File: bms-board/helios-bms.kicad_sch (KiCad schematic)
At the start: 61 parts, among them J1 Debug, J2 Umbilical, J3 Output, Q1 PMOS, Q2 NMOS, U1 TPS22811, U2 BQ25306, U3 STM32L011F4Ux, U4 THVD1400D, U6 TPS563207s

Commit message: components selected
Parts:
- removed J1: Debug, symbol Connector_Generic:Conn_01x05
- removed J2: Umbilical, symbol Connector_Generic:Conn_01x04
- added J1: Debug, Connector_PinHeader_1.27mm:PinHeader_2x05_P1.27mm_Vertical_SMD, symbol Connector_Generic:Conn_02x05_Odd_Even
- added J3: Umbilical, Connector_JST:JST_ZE_SM04B-ZESS-TB_1x04-1MP_P1.50mm_Horizontal, symbol Connector_Generic_MountingPin:Conn_01x04_MountingPin
- C1: renamed from C10; footprint (none) -> Capacitor_SMD:C_0603_1608Metric
- C10: renamed from C4; footprint (none) -> Capacitor_SMD:C_0603_1608Metric
- C11: renamed from C23; value 100u -> 470u; footprint (none) -> Capacitor_SMD:CP_Elec_10x10
- C12: renamed from C5; footprint (none) -> Capacitor_SMD:C_0402_1005Metric
- C13: renamed from C14; footprint (none) -> Capacitor_SMD:C_0402_1005Metric
- C14: renamed from C15; footprint (none) -> Capacitor_SMD:C_0402_1005Metric
- C15: renamed from C6; footprint (none) -> Capacitor_SMD:C_0402_1005Metric
- C16: renamed from C7; footprint (none) -> Capacitor_SMD:C_0402_1005Metric
- C17: renamed from C19; footprint (none) -> Capacitor_SMD:C_0603_1608Metric
- C18: renamed from C16; footprint (none) -> Capacitor_SMD:C_0402_1005Metric
- C19: renamed from C8; footprint (none) -> Capacitor_SMD:C_0603_1608Metric
- C2: renamed from C11; footprint (none) -> Capacitor_SMD:C_0402_1005Metric
- C20: renamed from C18; footprint (none) -> Capacitor_SMD:C_0402_1005Metric
- C21: renamed from C9; footprint (none) -> Capacitor_SMD:C_0603_1608Metric
- C22: renamed from C17; footprint (none) -> Capacitor_SMD:C_0603_1608Metric
- C23: renamed from C3; footprint (none) -> Capacitor_SMD:C_0402_1005Metric
- C3: renamed from C20; footprint (none) -> Capacitor_SMD:C_0402_1005Metric
- C4: renamed from C1; footprint (none) -> Capacitor_SMD:C_0402_1005Metric
- C5: renamed from C21; footprint (none) -> Capacitor_SMD:C_0402_1005Metric
- C6: renamed from C2; footprint (none) -> Capacitor_SMD:C_0402_1005Metric
- C7: renamed from C12; footprint (none) -> Capacitor_SMD:C_0402_1005Metric
- C8: renamed from C13; footprint (none) -> Capacitor_SMD:C_0603_1608Metric
- C9: renamed from C22; footprint (none) -> Capacitor_SMD:C_0402_1005Metric
- D1: footprint (none) -> LED_SMD:LED_0402_1005Metric
- J2: renamed from J3; footprint (none) -> Connector_JST:JST_ZE_SM03B-ZESS-TB_1x03-1MP_P1.50mm_Horizontal; symbol Connector_Generic:Conn_01x03 -> Connector_Generic_MountingPin:Conn_01x03_MountingPin
- L1: footprint (none) -> Inductor_SMD:L_Taiyo-Yuden_NR-50xx
- L2: footprint (none) -> Inductor_SMD:L_0805_2012Metric
- Q1: renamed from Q2; footprint (none) -> Helios-BMS:SOT-1220_UDFN6B_TOS-L; symbol Simulation_SPICE:NMOS -> Helios-BMS:SSM6K388NU
- Q2: renamed from Q1; value PMOS -> SSM3J332R; footprint (none) -> Helios-BMS:SOT-1220_UDFN6B_TOS-L; symbol Simulation_SPICE:PMOS -> Helios-BMS:SSM6J507NU
- R1: renamed from R23; footprint (none) -> Resistor_SMD:R_0402_1005Metric
- R10: renamed from R20; footprint (none) -> Resistor_SMD:R_0402_1005Metric
- R11: renamed from R21; value 50k -> 49.9k; footprint (none) -> Resistor_SMD:R_0402_1005Metric
- R12: renamed from R22; footprint (none) -> Resistor_SMD:R_0402_1005Metric
- R13: renamed from R10; footprint (none) -> Resistor_SMD:R_0402_1005Metric
- R14: renamed from R9; value TBD -> 300; footprint (none) -> Resistor_SMD:R_0402_1005Metric
- R15: renamed from R1; footprint (none) -> Resistor_SMD:R_0402_1005Metric
- R16: renamed from R2; footprint (none) -> Resistor_SMD:R_0402_1005Metric
- R17: renamed from R12; footprint (none) -> Resistor_SMD:R_0402_1005Metric
- R18: renamed from R11; footprint (none) -> Resistor_SMD:R_0402_1005Metric
- R19: renamed from R13; footprint (none) -> Resistor_SMD:R_0402_1005Metric
- R2: renamed from R3; footprint (none) -> Resistor_SMD:R_0402_1005Metric
- R20: renamed from R14; footprint (none) -> Resistor_SMD:R_0402_1005Metric
- R21: renamed from R15; footprint (none) -> Resistor_SMD:R_0402_1005Metric
- R22: renamed from R7; footprint (none) -> Resistor_SMD:R_0402_1005Metric
- R23: renamed from R8; footprint (none) -> Resistor_SMD:R_0402_1005Metric
- R24: footprint (none) -> Resistor_SMD:R_0402_1005Metric
- R3: renamed from R4; footprint (none) -> Resistor_SMD:R_0402_1005Metric
- R4: renamed from R17; footprint (none) -> Resistor_SMD:R_0402_1005Metric
- R5: renamed from R18; footprint (none) -> Resistor_SMD:R_0402_1005Metric
- R6: renamed from R19; footprint (none) -> Resistor_SMD:R_0402_1005Metric
- R7: renamed from R5; value 135k -> 137k; footprint (none) -> Resistor_SMD:R_0402_1005Metric
- R8: renamed from R6; footprint (none) -> Resistor_SMD:R_0402_1005Metric
- R9: renamed from R16; footprint (none) -> Resistor_SMD:R_0402_1005Metric
- U6: renamed from U4; footprint Package_TO_SOT_SMD:SOT-583-8 -> Package_SO:SOIC-8_3.9x4.9mm_P1.27mm
- renumbered U3 to U2, U1 to U3, U6 to U4, U2 to U5
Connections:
- net +12V: now also Q1.4 (S), J1.3 (Pin_3), J1.5 (Pin_5), J3.1 (Pin_1), J3.4 (Pin_4); no longer Q1.3 (S)
- net +3.3V: now also J1.1 (Pin_1)
- net +BATT: now also Q2.2 (D), Q2.5 (D), Q2.6 (D), Q2.7 (D)
- net DATA+: now also J3.3 (Pin_3)
- net DATA-: now also J3.2 (Pin_2)
- net EN/UVLO: now also Q1.2 (D), Q1.5 (D), Q1.6 (D)
- net GATE: now also Q1.3 (G); no longer Q1.2 (G)
- net SWCLK: now also J1.4 (Pin_4)
- net SWDIO: now also J1.2 (Pin_2)
- net VSYS: now also Q2.4 (S), Q2.8 (S); no longer Q2.3 (S)
- net ~{RESET}: now also J1.10 (Pin_10)
- net at D2.1 (K), R21.1: now also Q2.3 (G); no longer Q2.2 (G)
- new net: Q1.7, Q1.8
- no-connect marks 12 -> 18
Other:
- note added: "4.8V PGTH Eq. 13: 4.8V = 1.2V (Rtop + Rbot)/Rbot -> 4 = Rtop+Rbot/Rbot Rtop = 150k, Rbot = 50k 4.8V/(Rtop + Rbot) = 24uA >20x than PGTH leakage current 49.9k for sourcing reasons"
- note added: "Changed from recommended value to account for sourcing. Increases output to 3.34V"
- note removed: "4.8V PGTH Eq. 13: 4.8V = 1.2V (Rtop + Rbot)/Rbot -> 4 = Rtop+Rbot/Rbot Rtop = 150k, Rbot = 50k 4.8V/(Rtop + Rbot) = 24uA >20x than PGTH leakage current"
- moved on the sheet: C13, C18, U2

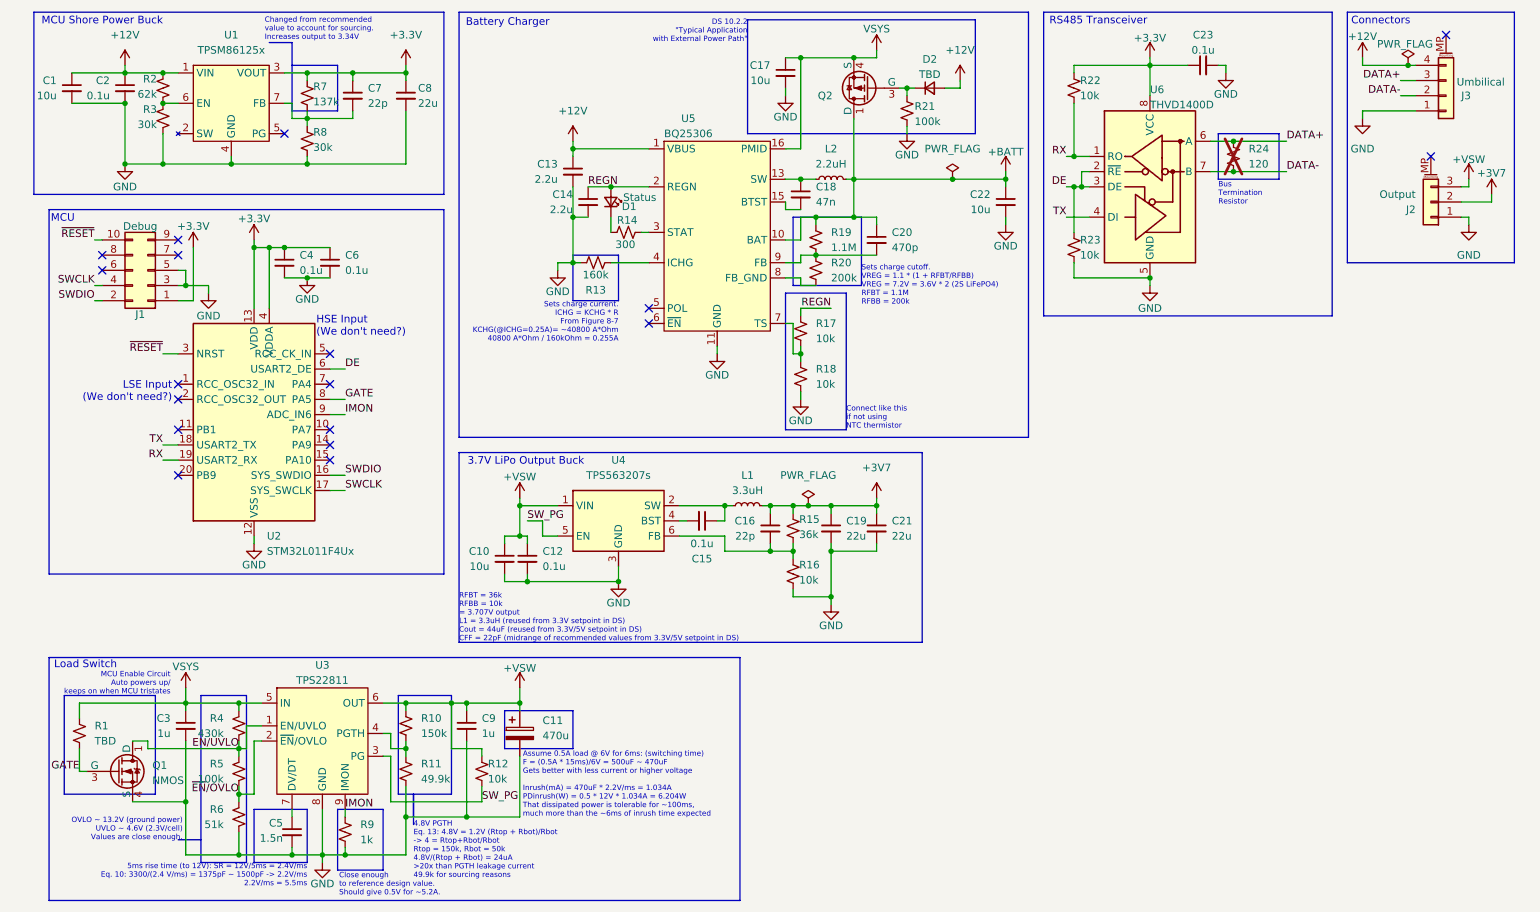
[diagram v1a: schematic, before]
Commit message: fixed ERC errors
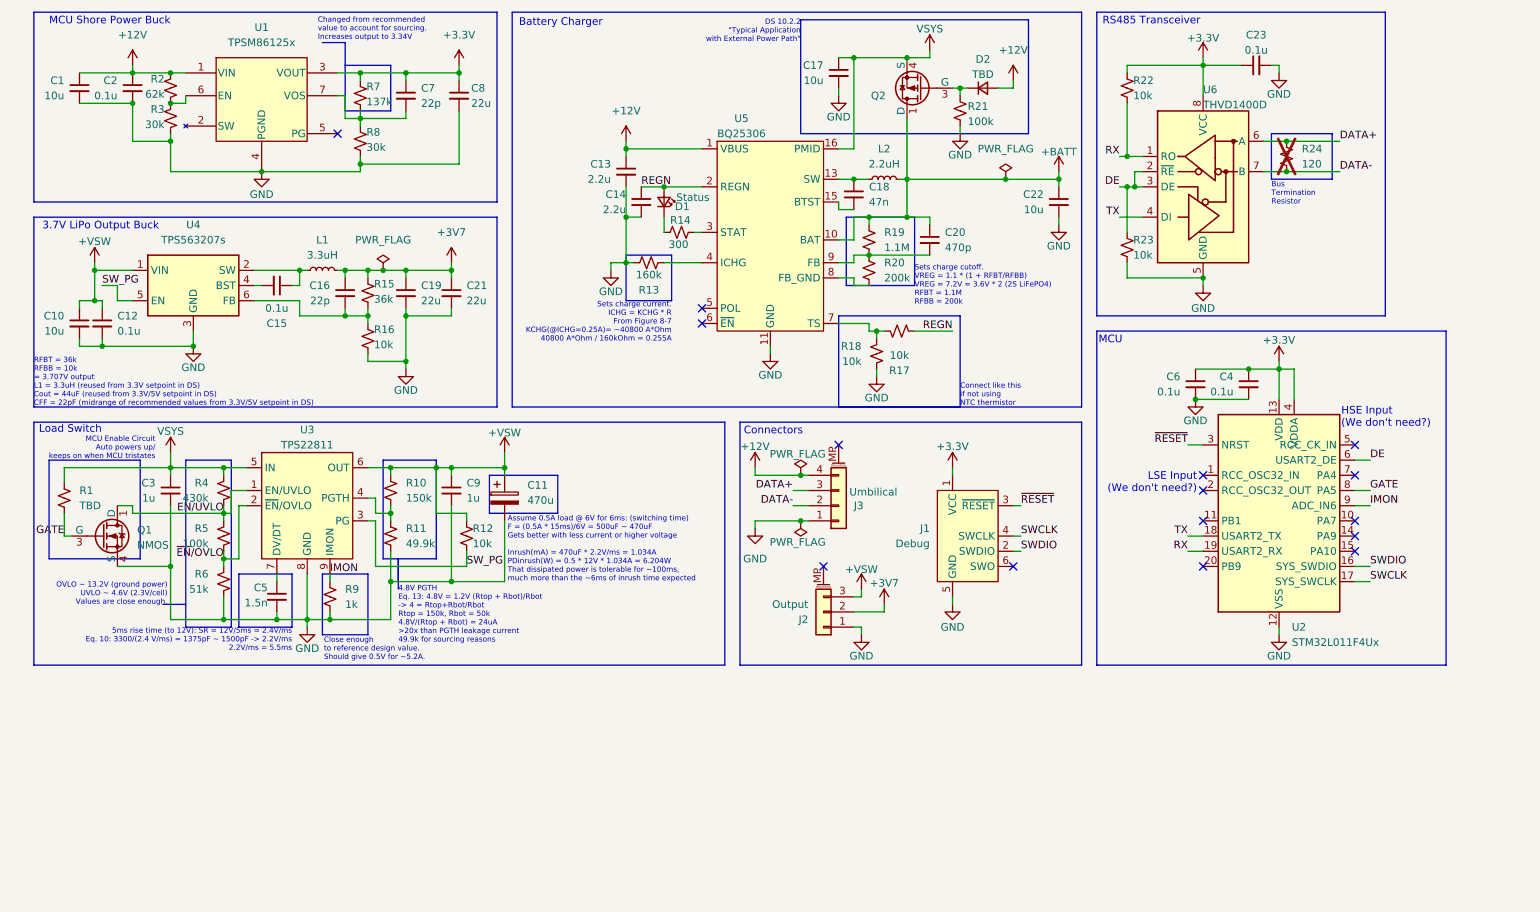
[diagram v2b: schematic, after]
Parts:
- removed J1: Debug, Connector_PinHeader_1.27mm:PinHeader_2x05_P1.27mm_Vertical_SMD, symbol Connector_Generic:Conn_02x05_Odd_Even
- added J1: Debug, Connector:Tag-Connect_TC2030-IDC-NL_2x03_P1.27mm_Vertical, symbol Connector:Conn_ARM_SWD_TagConnect_TC2030-NL
- added U1: TPSM86125x, Helios-BMS:Texas-QFN-FCMOD-7_4x3.3mm, symbol Helios-BMS:TPSM861253RDXR
- D2: footprint (none) -> Diode_SMD:D_0402_1005Metric
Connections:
- net +12V: now also U1.1 (VIN); no longer C1.2, C10.2, C11.2, C12.2, C13.2, C14.2, C17.2, C19.2, C2.2, C21.2, C22.2, C23.2, C3.2, C4.2, C5.2, C6.2, C8.2, C9.2, J2.1 (Pin_1), J3.1 (Pin_1), Q1.4 (S), R11.2, R13.2, R16.2, R18.2, R21.2, R23.2, R3.2, R6.2, R8.2, R9.2, U2.12 (VSS), U3.8 (GND), U4.3 (GND), U5.11 (GND), U5.12 (GND), U5.17 (GND), U6.5 (GND)
- net +3.3V: now also J1.1 (VCC), U1.3 (VOUT)
- net REGN: now also R17.2; no longer R17.1
- net SWCLK: now also J1.4 (SWCLK)
- net SWDIO: now also J1.2 (SWDIO)
- net ~{RESET}: now also J1.3 (~{RESET})
- net at C7.2, R7.2, R8.1: now also U1.7 (VOS)
- net at R18.1, U5.7 (TS): now also R17.1; no longer R17.2
- net at R2.2, R3.1: now also U1.6 (EN)
- new net GND: C1.2, C10.2, C11.2, C12.2, C13.2, C14.2, C17.2, C19.2, C2.2, C21.2, C22.2, C23.2, C3.2, C4.2, C5.2, C6.2, C8.2, C9.2, J1.5 (GND), J2.1 (Pin_1), J3.1 (Pin_1), Q1.4 (S), R11.2, R13.2, R16.2, R18.2, R21.2, R23.2, R3.2, R6.2, R8.2, R9.2, U1.4 (PGND), U2.12 (VSS), U3.8 (GND), U4.3 (GND), U5.11 (GND), U5.12 (GND), U5.17 (GND), U6.5 (GND)
- no-connect marks 18 -> 15
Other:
- moved on the sheet: C1, C10, C11, C12, C13, C14, C15, C16, C17, C18, C19, C2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

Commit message: routed 2layer 2oz, gonna change to 4layer 1oz
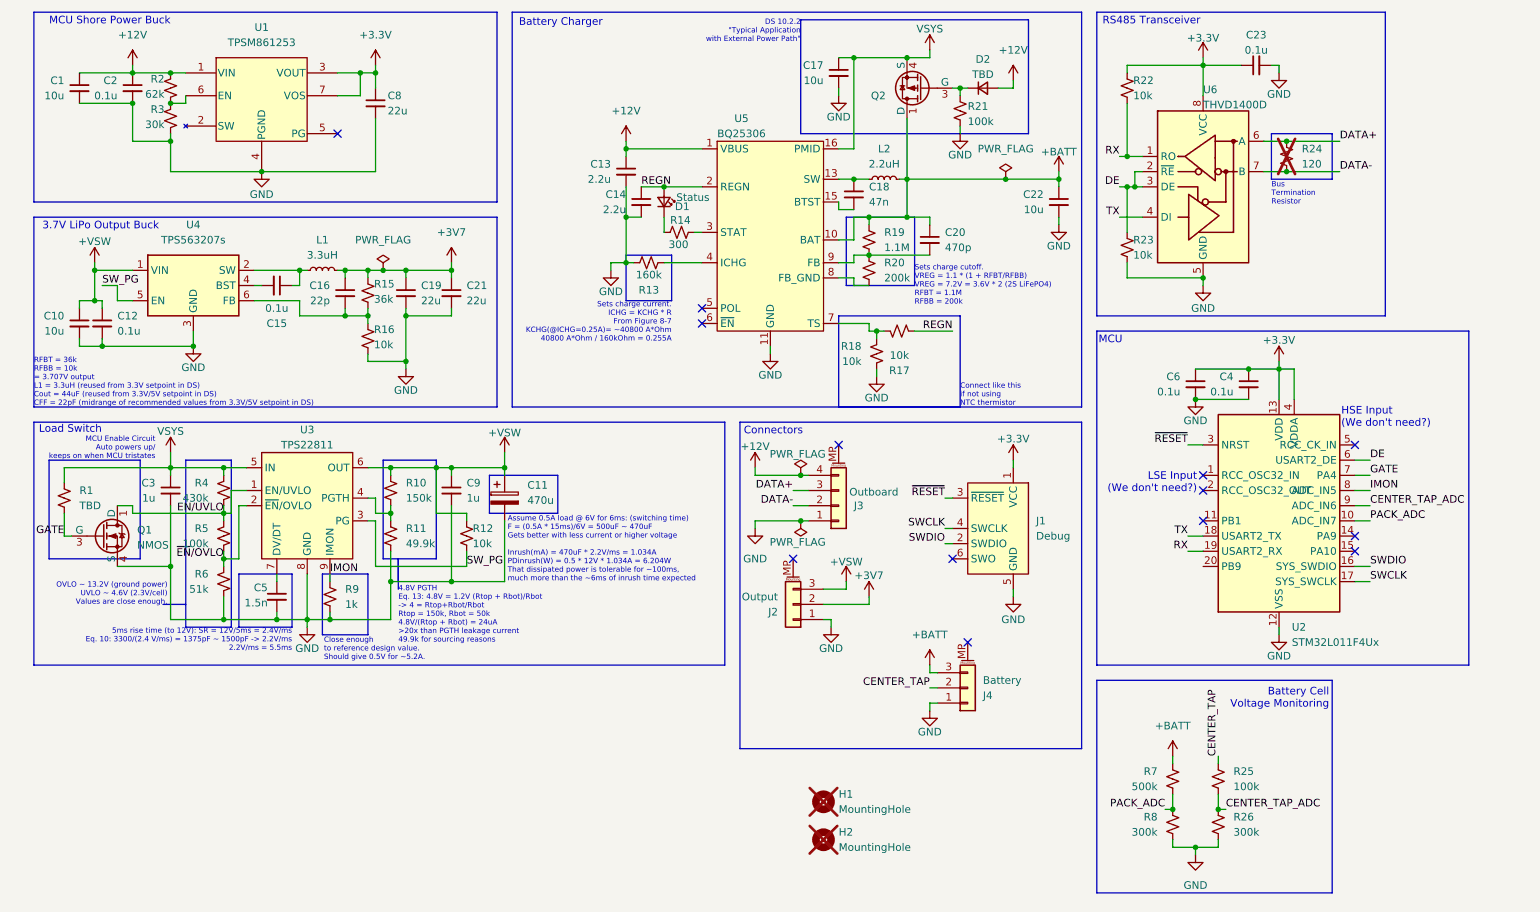
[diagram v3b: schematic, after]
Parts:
- removed C7: 22p, Capacitor_SMD:C_0402_1005Metric, symbol Device:C_Small
- added H1, H2: MountingHole, MountingHole:MountingHole_3.2mm_M3_DIN965, symbol Mechanical:MountingHole
- added J4: Battery, Connector_JST:JST_ZE_SM03B-ZESS-TB_1x03-1MP_P1.50mm_Horizontal, symbol Connector_Generic_MountingPin:Conn_01x03_MountingPin
- added R25: 100k, Resistor_SMD:R_0402_1005Metric, symbol Device:R_Small_US
- added R26: 300k, Resistor_SMD:R_0402_1005Metric, symbol Device:R_Small_US
- C11: footprint Capacitor_SMD:CP_Elec_10x10 -> Capacitor_THT:CP_Radial_D6.3mm_P2.50mm
- J3: value Umbilical -> Outboard
- L1: footprint Inductor_SMD:L_Taiyo-Yuden_NR-50xx -> Inductor_SMD:L_1008_2520Metric
- R7: value 137k -> 500k
- R8: value 30k -> 300k
- U1: value TPSM86125x -> TPSM861253
- U6: footprint Package_SO:SOIC-8_3.9x4.9mm_P1.27mm -> Package_TO_SOT_SMD:SOT-583-8
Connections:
- net +3.3V: now also U1.7 (VOS); no longer R7.1
- net +BATT: now also R7.1, J4.3 (Pin_3)
- net GATE: now also U2.7 (PA4); no longer U2.8 (PA5)
- net GND: now also J4.1 (Pin_1), R26.2
- net IMON: now also U2.8 (PA5); no longer U2.9 (PA6)
- net PACK_ADC: now reaches R7.2, R8.1
- net PACK_ADC: now also U2.10 (PA7); no longer U1.7 (VOS)
- new net CENTER_TAP: J4.2 (Pin_2), R25.1
- new net CENTER_TAP_ADC: R25.2, R26.1, U2.9 (PA6)
- no-connect marks 15 -> 13
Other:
- note added: "Battery Cell Voltage Monitoring"
- note removed: "Changed from recommended value to account for sourcing. Increases output to 3.34V"
- moved on the sheet: C8, J1, J2

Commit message: rerouted for 4 layers
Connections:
- net CENTER_TAP_ADC: now also U2.8 (PA5); no longer U2.9 (PA6)
- net GATE: now also U2.10 (PA7); no longer U2.7 (PA4)
- net IMON: now also U2.9 (PA6); no longer U2.8 (PA5)
- net PACK_ADC: now also U2.7 (PA4); no longer U2.10 (PA7)
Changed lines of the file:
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@@
 	)
 	(label "IMON"
-		(at 237.49 93.98 0)
+		(at 237.49 96.52 0)
 		(effects
 			(font
@@
 	)
 	(label "CENTER_TAP_ADC"
-		(at 237.49 96.52 0)
+		(at 237.49 93.98 0)
 		(effects
 			(font
@@
 	)
 	(label "GATE"
-		(at 237.49 91.44 0)
+		(at 237.49 99.06 0)
 		(effects
 			(font
@@
 	)
 	(label "PACK_ADC"
-		(at 237.49 99.06 0)
+		(at 237.49 91.44 0)
 		(effects
 			(font
